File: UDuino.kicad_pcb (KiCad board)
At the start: 4 copper layers, 119.4 x 119.4 mm, 124 parts, among them J101 Barrel_Jack, J102 Conn_01x02_Female, J103 PMOD1, J104 Conn_01x03_Male, J105 Conn_01x03_Male, J106 Conn_01x04_Male, J107 Conn_01x04_Male, J301 Screw_Terminal_01x04, P1401 USB_C_Plug, Q901 TRANS_PNP-MMBT4403, Q902 TRANS_PNP-MMBT4403, Q903 TRANS_PNP-MMBT4403, Q904 TRANS_PNP-MMBT4403, U101 STM32L452VCTx, U1201 AP63205WU, U1301 AP63203WU, U301 DRV8833RTY, U401 NAU8315YG, U501 NAU8315YG

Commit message: Feb 12 2023 Week Work
Remaining Things to accomplish
Audio connect to Microcontroller
7-Seg connect to Microcontroller
PMOD connect to Microcontroller
Misc Microcontroller items, like reset and boot buttons
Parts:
- moved C105 55.8 mm to (25.1, 81.5)
- moved C107 53.3 mm to (30.5, 74.9), turned to 0 degrees
- moved C106 52.6 mm to (24.9, 74.9)
- moved C101 52.3 mm to (25.1, 77.0), turned to 180 degrees
- moved C102 51.7 mm to (30.2, 81.0), turned to 0 degrees
- moved C108 48.8 mm to (30.5, 76.7), turned to 0 degrees
- moved C103 48.3 mm to (25.1, 79.2)
- moved C109 46.6 mm to (30.2, 83.3)
- moved C104 46.3 mm to (30.2, 78.7), turned to 0 degrees
- moved C110 43.0 mm to (24.9, 83.6), turned to 0 degrees
- moved C1204 35.6 mm to (11.4, 102.6)
- moved L1201 35.6 mm to (10.9, 100.3)
- moved C1201 35.6 mm to (15.2, 103.3)
- moved C1202 35.6 mm to (13.2, 97.5)
- moved C1203 35.6 mm to (11.4, 104.4)
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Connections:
- net /SIA1_SCK__A renamed /SAI1_SCK__A
- net /SIA_SD_B renamed /SAI_SD_B
- U101 pad 3: /SIA1_FS_A -> /SAI1_FS_A
- U101 pad 5: /SIA1_SD_A -> /SAI1_SD_A
- U101 pad 70: /USB_DM -> /USB_DN
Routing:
- net +3V3: track 78.3 -> 553.8 mm, vias 18 -> 14
- net +5V: track 14.5 -> 220.9 mm, vias 3 -> 7
- net /V_IN: track 5.73 -> 193.0 mm, vias 1 -> 2
- net /Speaker Left/GAIN: track 3.74 -> 117.3 mm
- net /D2: track 42.2 -> 150.9 mm
- net /D3: track 35.0 -> 141.7 mm
- net /BTN4: track 6.59 -> 101.6 mm
- net /SPI3_MOSI: track 2.10 -> 89.6 mm, vias 1 -> 2
- net /BTN5: track 7.91 -> 95.4 mm, vias 2 -> 3
- net /SPI3_SCK: track 1.33 -> 88.6 mm, vias 1 -> 2
- net /LCD-NCSB: track 2.09 -> 78.8 mm
- net /LCD-RS: track 2.75 -> 75.5 mm
- net /LED7: track 2.68 -> 61.4 mm
- net /USB_DN: track 0.00 -> 56.3 mm, vias 0 -> 2
- net /UART4_RX: track 2.09 -> 58.1 mm, vias 1 -> 2
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
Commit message: REVISION 0 DONE
Done first revision of the UDUINO
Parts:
- removed C110: 1u, Capacitor_SMD:C_0603_1608Metric
- added R101: 10k, Resistor_SMD:R_0603_1608Metric, F.Cu at (35.4, 93.6)
- added S101: PTS636_SM43_SMTR_LFS, Custom:PTS636SM43SMTRLFS, F.Cu at (39.8, 97.8)
- added S102: PTS636_SM43_SMTR_LFS, Custom:PTS636SM43SMTRLFS, F.Cu at (46.6, 97.9)
- C101: moved to F.Cu
- C105, C109: value 100n -> 4u7; footprint Capacitor_SMD:C_0805_2012Metric -> Capacitor_SMD:C_0603_1608Metric
- C107: value 10n -> 100n; footprint Capacitor_SMD:C_0603_1608Metric -> Capacitor_SMD:C_0805_2012Metric
- C108: value 1u -> 100n; footprint Capacitor_SMD:C_0603_1608Metric -> Capacitor_SMD:C_0805_2012Metric
- U101: value STM32L452VCTx -> STM32F072VBTx
- moved C101 14.4 mm to (39.1, 80.3), turned to 90 degrees
- moved MK601 11.9 mm to (110.5, 35.8), turned to -90 degrees
- moved C602 11.7 mm to (115.3, 35.8), turned to -90 degrees
- moved C202 10.8 mm to (12.4, 35.6), turned to -90 degrees
- moved C601 10.5 mm to (113.7, 35.8), turned to 90 degrees
- moved MK201 8.98 mm to (7.62, 35.6), turned to -90 degrees
- moved C201 8.92 mm to (10.8, 35.6), turned to 90 degrees
- moved C107 8.66 mm to (22.1, 77.1), turned to 180 degrees
- moved C108 8.57 mm to (22.1, 74.9), turned to 180 degrees
- moved C102 7.98 mm to (22.4, 82.7), turned to 180 degrees
- moved C103 5.77 mm to (28.8, 74.8), turned to 0 degrees
- moved R601 5.06 mm to (113.0, 38.6), turned to 180 degrees
- moved C106 4.44 mm to (29.0, 76.7), turned to 0 degrees
- moved C104 4.18 mm to (28.8, 82.7)
- moved C105 2.90 mm to (22.4, 80.8)
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- renumbered R703 to R701, R704 to R702, R705 to R703, R706 to R704, R707 to R705, R708 to R706, R701 to R707, R702 to R708
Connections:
- A101 pad D0: /UART4_RX -> /UART_RX
- A101 pad D1: /UART4_TX -> /UART_TX
- C101 pad 2: +3V3 -> /NRST
- C109 pad 1: +3V3 -> GND
- C109 pad 2: GND -> +3V3
- DS1101 pad 5: /SPI3_SCK -> /SPI1_SCK
- DS1101 pad 6: /SPI3_MOSI -> /SPI1_MOSI
- J106 pad 3: /D2 -> /D3
- J106 pad 4: /D3 -> /D2
- J107 pad 3: /D4 -> /D5
- J107 pad 4: /D5 -> /D4
- MK201 pad 3: /SAI1_FS_A -> /I2S2_WS
- MK201 pad 6: /SAI1_SCK_A -> /I2S2_CK
- MK201 pad 7: /SIA1_SD_B -> /I2S2_SD
- MK601 pad 3: /SAI1_FS_A -> /I2S2_WS
- MK601 pad 6: /SAI1_SCK_A -> /I2S2_CK
- MK601 pad 7: /SIA1_SD_B -> /I2S2_SD
- R201 pad 2: /SIA1_SD_B -> /I2S2_SD
- R601 pad 2: /SIA1_SD_B -> /I2S2_SD
- U101 pad 1: /BIN2 -> /LED3
- U101 pad 10: GND -> /PMOD_8
- U101 pad 11: +3V3 -> /PMOD_7
- U101 pad 15: /LED1 -> /PMOD_6
- U101 pad 16: /LED2 -> /PMOD_5
- U101 pad 17: /LED3 -> /PMOD_4
- U101 pad 18: /LED4 -> /PMOD_3
- U101 pad 19: GND -> /PMOD_2
- U101 pad 2: /BIN1 -> /LED4
- U101 pad 22: +3V3 -> /PMOD_1
- U101 pad 23: /UART4_TX -> /7Seg-AN1
- U101 pad 24: /UART4_RX -> /7Seg-AN2
- U101 pad 25: /A0 -> /7Seg-AN3
- U101 pad 26: /A1 -> /7Seg-AN4
- U101 pad 29: /A2 -> /I2S1_WS
- U101 pad 3: /SAI1_FS_A -> /LED5
- U101 pad 30: /A3 -> /I2S1_CK
- U101 pad 31: /A4 -> /A3
- U101 pad 32: /A5 -> /I2S1_SD
- U101 pad 33: /LED5 -> /7Seg-A
- U101 pad 34: /LED6 -> /7Seg-B
- U101 pad 35: /PMOD4 -> /7Seg-C
- U101 pad 36: /LCD-RS -> /7Seg-D
- U101 pad 37: /LCD-NCSB -> /7Seg-E
- U101 pad 38: /SAI_SD_B -> /7Seg-F
- U101 pad 39: /PMOD_6 -> /7Seg-G
- U101 pad 4: /SAI1_SCK__A -> /LED6
- U101 pad 40: /PMOD_7 -> /7Seg-DP
- U101 pad 41: /D2 -> /A4
- U101 pad 42: /D3 -> /LCD-RS
- U101 pad 43: /D4 -> /LCD-NCSB
- U101 pad 44: /D5 -> /SPI1_SCK
- U101 pad 45: /D6 -> /SPI1_MISO
- U101 pad 46: /D7 -> /SPI1_MOSI
- U101 pad 47: /BTN4 -> /UART_TX
- U101 pad 48: /BTN5 -> /UART_RX
- U101 pad 5: /SAI1_SD_A -> /LED7
- U101 pad 51: /7Seg-AN1 -> /I2S2_WS
- U101 pad 52: /7Seg-AN2 -> /I2S2_CK
- U101 pad 53: /7Seg-AN3 -> /A5
- U101 pad 54: /7Seg-AN4 -> /I2S2_SD
- U101 pad 55: /D8 -> /D2
- U101 pad 56: /D9 -> /D3
- U101 pad 57: /D10 -> /D4
- U101 pad 58: /D11 -> /D5
- U101 pad 59: /I2C4_SCL -> /D6
- U101 pad 60: /I2C4_SDA -> /D7
- U101 pad 61: /D12 -> /D8
- U101 pad 62: /D13 -> /D9
- U101 pad 63: /LED7 -> /D10
- U101 pad 64: /LED8 -> /D11
- U101 pad 65: /7Seg-A -> /D12
- U101 pad 66: /7Seg-B -> /D13
- U101 pad 67: /PMOD_1 -> /NSLEEP
- U101 pad 68: /PMOD2 -> /AIN1
- U101 pad 69: /PMOD_3 -> /AIN2
- U101 pad 7: /7Seg-F -> /LED8
- U101 pad 72: /SYS_JTMS-SWDIO -> /BIN2
- U101 pad 73: /V_USB -> /BIN1
- U101 pad 76: /SYS_JTCK-SWCLK -> /NFAULT
- U101 pad 77: /SYS_JTDI -> unconnected-(U101-Pad77)
- U101 pad 78: /7Seg-C -> /A0
- U101 pad 79: /7Seg-D -> /A1
- U101 pad 8: /7Seg-G -> unconnected-(U101-Pad8)
- U101 pad 80: /7Seg-E -> /A2
- U101 pad 89: /SPI3_SCK -> /BTN1
- U101 pad 9: /7Seg-DP -> unconnected-(U101-Pad9)
- U101 pad 90: /SPI3_MISO -> /BTN2
- U101 pad 91: /SPI3_MOSI -> /BTN3
- U101 pad 92: /PMOD_5 -> /I2C1_SDA
- U101 pad 93: /BTN1 -> /I2C1_SCL
- U101 pad 94: unconnected-(U101-Pad94) -> /BOOT
- U101 pad 95: /BTN2 -> /BTN4
- U101 pad 96: /BTN3 -> /BTN5
- U101 pad 97: /AIN1 -> /LED1
- U101 pad 98: /AIN2 -> /LED2
- U301 pad 15: /D3 -> /NSLEEP
- U301 pad 6: /D2 -> /NFAULT
- U401 pad 6: /SAI1_SCK_A -> /I2S1_CK
- U401 pad 8: /SAI1_FS_A -> /I2S1_WS
- U401 pad 9: /SAI1_SD_A -> /I2S1_SD
- U501 pad 6: /SAI1_SCK_A -> /I2S1_CK
- U501 pad 7: /SAI1_FS_A -> /I2S1_WS
- U501 pad 9: /SAI1_SD_A -> /I2S1_SD
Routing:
- net /I2S2_SD: track 0.00 -> 168.6 mm, vias 0 -> 4
- net /I2S2_WS: track 0.00 -> 158.2 mm, vias 0 -> 4
- net /I2S2_CK: track 0.00 -> 155.5 mm, vias 0 -> 4
- net /I2S1_WS: track 0.00 -> 151.9 mm, vias 0 -> 4
- net /I2S1_SD: track 0.00 -> 149.0 mm, vias 0 -> 4
- net /I2S1_CK: track 0.00 -> 149.0 mm, vias 0 -> 4
- net +3V3: track 553.8 -> 682.3 mm, vias 14 -> 17
- net /NSLEEP: track 0.00 -> 118.4 mm, vias 0 -> 2
- net /PMOD_5: track 1.47 -> 119.6 mm
- net /D2: track 150.9 -> 35.2 mm, vias 2 -> 1
- net /PMOD_1: track 1.47 -> 116.0 mm
- net /PMOD_6: track 1.33 -> 113.9 mm
- net /PMOD_8: track 0.00 -> 111.3 mm, vias 0 -> 1
- net /PMOD_2: track 0.00 -> 111.0 mm, vias 0 -> 2
- net /PMOD_3: track 2.76 -> 111.8 mm, vias 1 -> 2
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
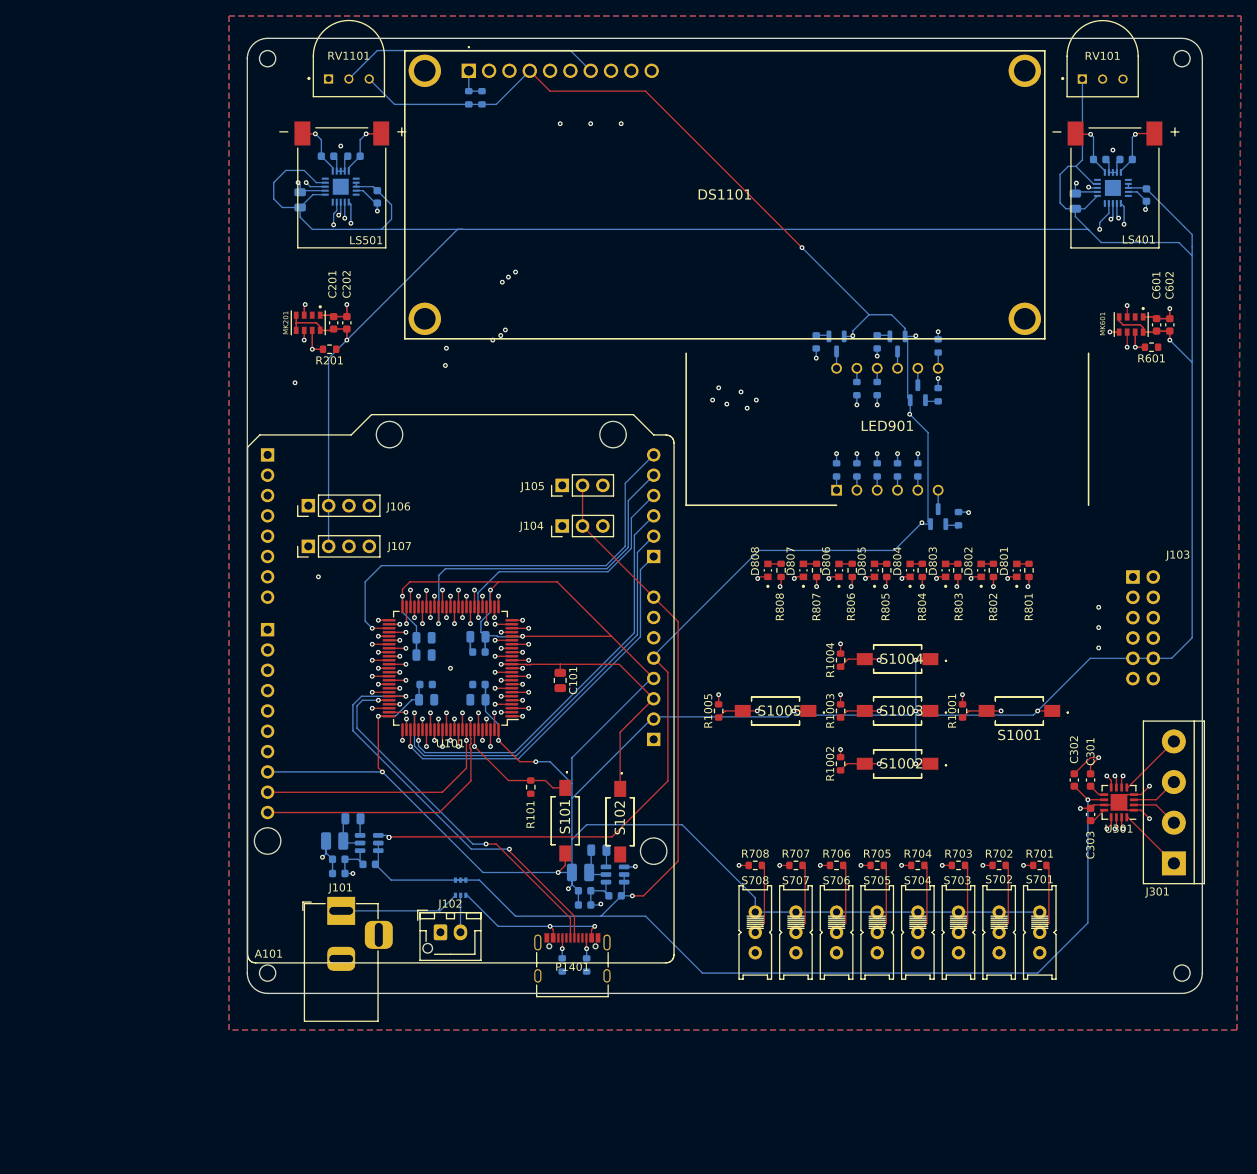
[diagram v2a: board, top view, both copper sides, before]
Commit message: DRC checks done, GRBL files made
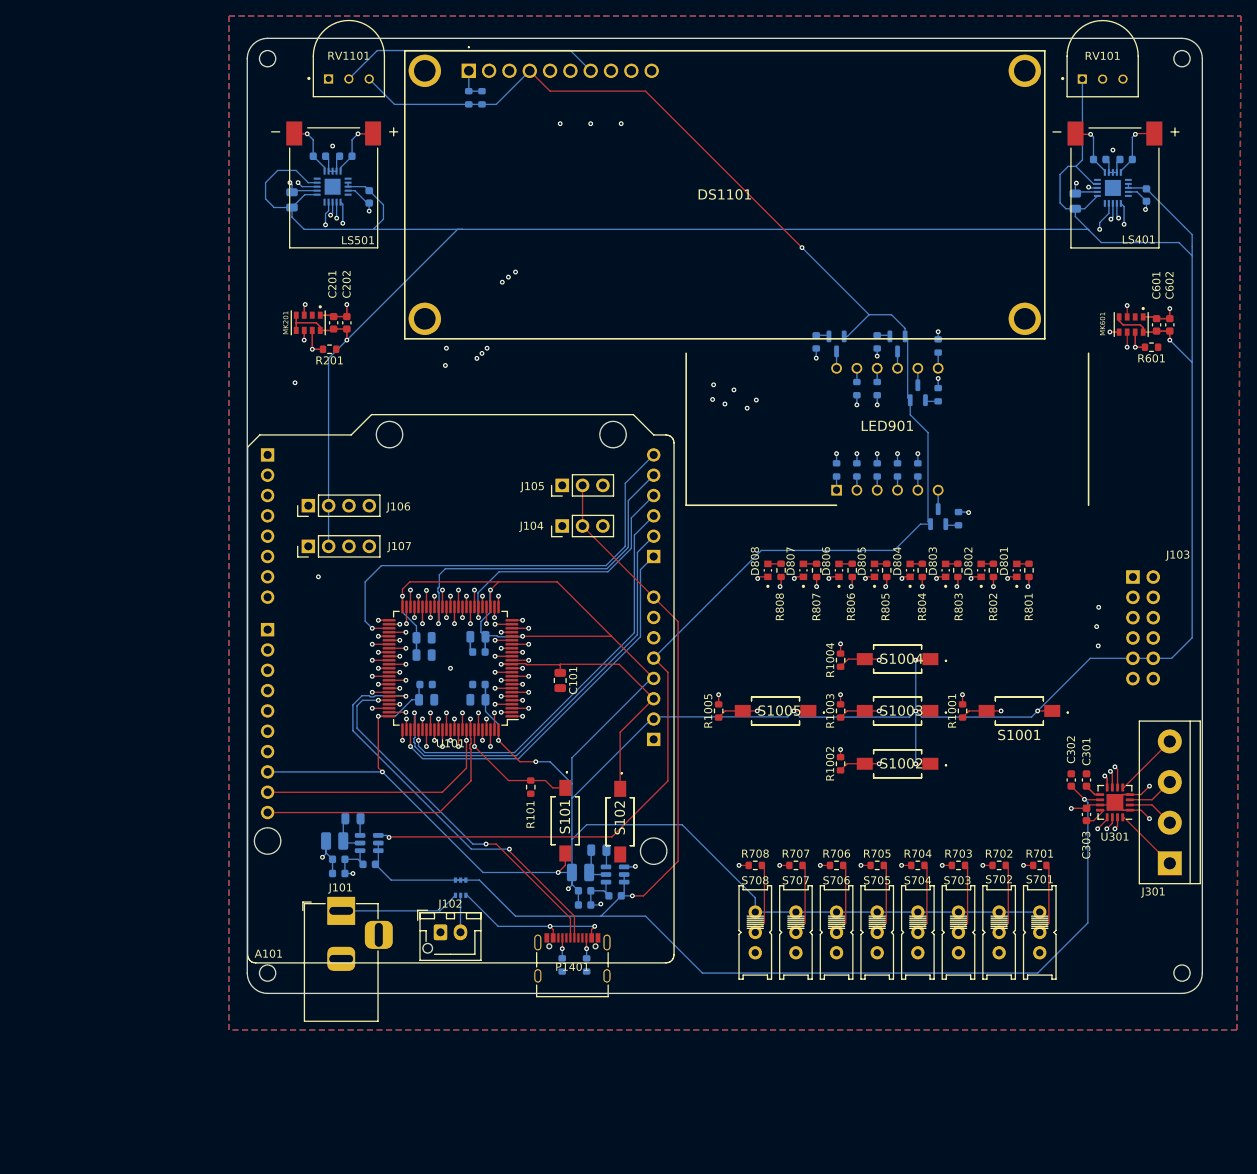
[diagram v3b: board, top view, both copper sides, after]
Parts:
- moved C501 1.02 mm to (15.2, 19.8)
- moved C502 1.02 mm to (5.59, 20.2)
- moved C503 1.02 mm to (12.3, 14.7)
- moved C504 1.02 mm to (9.02, 14.7)
- moved LS501 1.02 mm to (10.8, 18.7)
- moved U501 1.02 mm to (10.7, 18.5)
- moved C301 0.51 mm to (104.9, 92.7)
- moved C303 0.51 mm to (104.9, 97.0)
- moved J301 0.51 mm to (115.3, 103.1)
- moved U301 0.51 mm to (108.5, 95.5)
- moved C302 0.38 mm to (103.0, 92.7)
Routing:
- net GND: track 103.9 -> 100.0 mm, vias 41 -> 40
- net +5V: track 228.1 -> 226.2 mm, vias 8 -> 3
- net /Speaker Left/GAIN: track 117.3 -> 118.4 mm
- net /PMOD_1: track 116.0 -> 117.0 mm
- net +3V3: track 682.3 -> 683.3 mm
- net /AIN2: track 113.2 -> 112.3 mm
- net /PMOD_3: track 111.8 -> 112.6 mm
- net /NSLEEP: track 118.4 -> 117.6 mm
- net /PMOD_2: track 111.0 -> 111.8 mm
- net /NFAULT: track 105.7 -> 105.0 mm
- net /AIN1: track 118.6 -> 118.0 mm
- net /I2S1_SD: track 149.0 -> 149.6 mm
- net /7Seg-A: track 75.4 -> 74.9 mm
- net /7Seg-DP: track 81.5 -> 82.0 mm
- net /7Seg-G: track 88.3 -> 88.9 mm
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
